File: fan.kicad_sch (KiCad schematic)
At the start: 20 parts, among them J5 Conn_01x04, J6 Conn_01x04, U15 TMP1075, U16 TMP1075, U17 EMC2302, U18 EMC2101

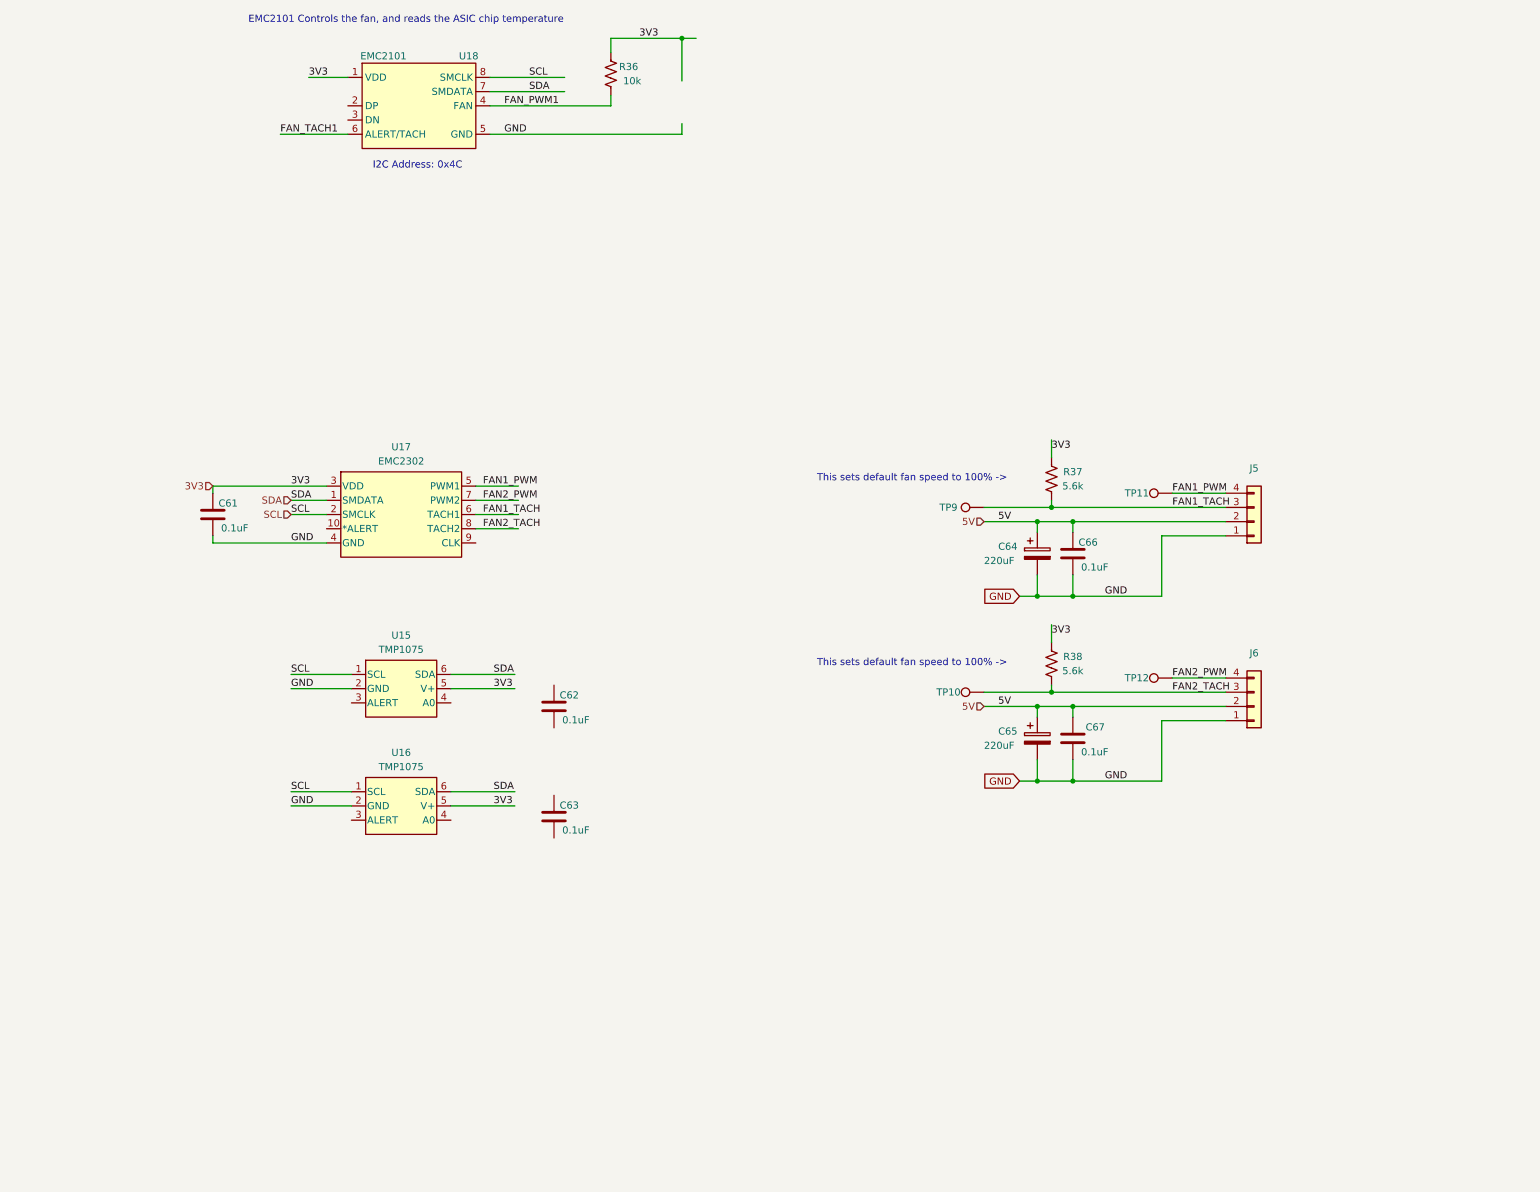
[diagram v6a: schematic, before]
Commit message: add level translator circuits to ASIC communications
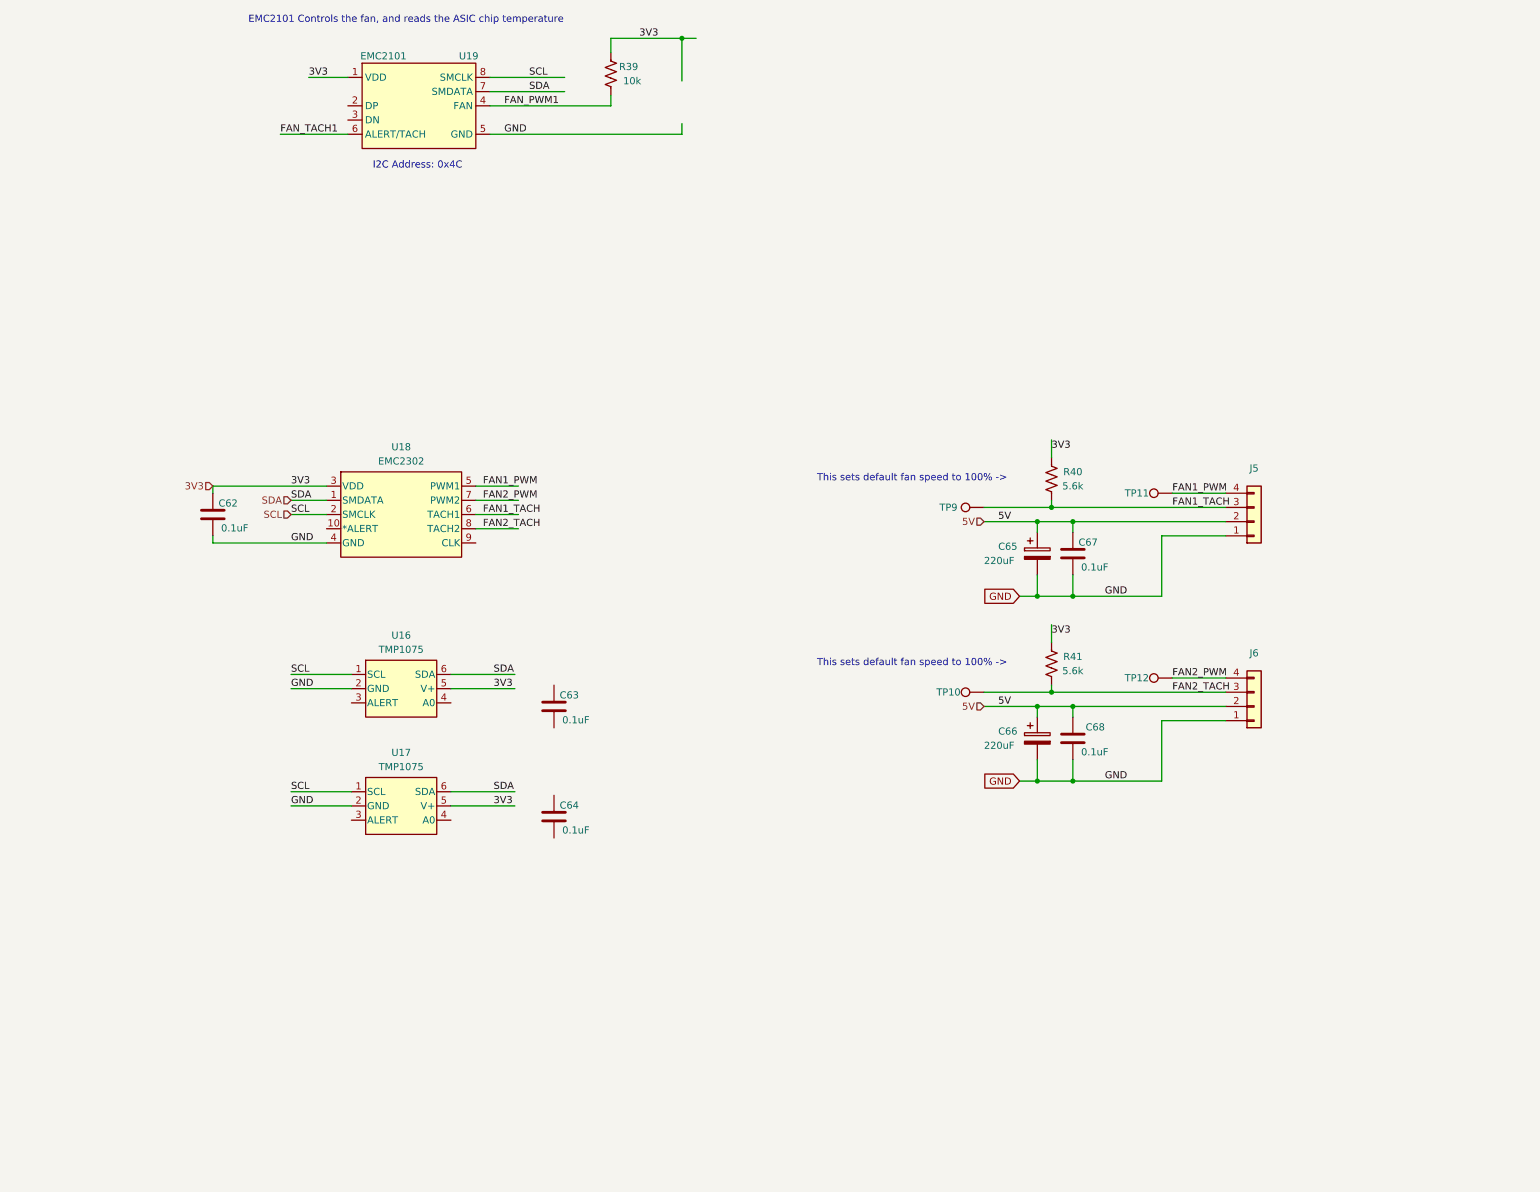
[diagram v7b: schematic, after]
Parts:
- renumbered C61 to C62, C62 to C63, C63 to C64, C64 to C65, C65 to C66, C66 to C67, C67 to C68, R36 to R39, R37 to R40, R38 to R41, U15 to U16, U16 to U17, U17 to U18, U18 to U19
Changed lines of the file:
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@@
   (symbol (lib_id "bitaxe:EMC2302-2-AIZL-TR") (at 89.535 52.07 0) (unit 1)
     (in_bom yes) (on_board yes) (dnp no) (fields_autoplaced)
-    (property "Reference" "U17" (at 91.44 40.005 0)
+    (property "Reference" "U18" (at 91.44 40.005 0)
       (effects (font (size 1.27 1.27)))
     )
@@
       (project "bitaxeUltraHex"
         (path "/e63e39d7-6ac0-4ffd-8aa3-1841a4541b55/8e8832ea-6bf1-49d2-b3a5-32a207f555d2"
-          (reference "U17") (unit 1)
+          (reference "U18") (unit 1)
         )
       )
@@
   (symbol (lib_id "Device:C_Polarized") (at 205.105 92.075 0) (unit 1)
     (in_bom yes) (on_board yes) (dnp no)
-    (property "Reference" "C65" (at 198.12 90.805 0)
+    (property "Reference" "C66" (at 198.12 90.805 0)
       (effects (font (size 1.27 1.27)) (justify left))
     )
@@
       (project "bitaxeUltraHex"
         (path "/e63e39d7-6ac0-4ffd-8aa3-1841a4541b55/8e8832ea-6bf1-49d2-b3a5-32a207f555d2"
-          (reference "C65") (unit 1)
+          (reference "C66") (unit 1)
         )
       )
@@
   (symbol (lib_id "Device:R_US") (at 207.645 45.72 180) (unit 1)
     (in_bom yes) (on_board yes) (dnp no)
-    (property "Reference" "R37" (at 211.455 44.45 0)
+    (property "Reference" "R40" (at 211.455 44.45 0)
       (effects (font (size 1.27 1.27)))
     )
@@
       (project "bitaxeUltraHex"
         (path "/e63e39d7-6ac0-4ffd-8aa3-1841a4541b55/8e8832ea-6bf1-49d2-b3a5-32a207f555d2"
-          (reference "R37") (unit 1)
+          (reference "R40") (unit 1)
         )
       )
@@
   (symbol (lib_id "Device:C") (at 118.745 86.36 0) (mirror y) (unit 1)
     (in_bom yes) (on_board yes) (dnp no)
-    (property "Reference" "C62" (at 123.19 85.09 0)
+    (property "Reference" "C63" (at 123.19 85.09 0)
       (effects (font (size 1.27 1.27)) (justify left bottom))
     )
@@
       (project "bitaxeUltraHex"
         (path "/e63e39d7-6ac0-4ffd-8aa3-1841a4541b55/8e8832ea-6bf1-49d2-b3a5-32a207f555d2"
-          (reference "C62") (unit 1)
+          (reference "C63") (unit 1)
         )
       )
@@
   (symbol (lib_id "Device:C") (at 57.785 52.07 0) (mirror y) (unit 1)
     (in_bom yes) (on_board yes) (dnp no)
-    (property "Reference" "C61" (at 62.23 50.8 0)
+    (property "Reference" "C62" (at 62.23 50.8 0)
       (effects (font (size 1.27 1.27)) (justify left bottom))
     )
@@
       (project "bitaxeUltraHex"
         (path "/e63e39d7-6ac0-4ffd-8aa3-1841a4541b55/8e8832ea-6bf1-49d2-b3a5-32a207f555d2"
-          (reference "C61") (unit 1)
+          (reference "C62") (unit 1)
         )
       )
@@
   (symbol (lib_id "Device:C") (at 211.455 59.055 0) (mirror y) (unit 1)
     (in_bom yes) (on_board yes) (dnp no)
-    (property "Reference" "C66" (at 215.9 57.785 0)
+    (property "Reference" "C67" (at 215.9 57.785 0)
       (effects (font (size 1.27 1.27)) (justify left bottom))
     )
@@
       (project "bitaxeUltraHex"
         (path "/e63e39d7-6ac0-4ffd-8aa3-1841a4541b55/8e8832ea-6bf1-49d2-b3a5-32a207f555d2"
-          (reference "C66") (unit 1)
+          (reference "C67") (unit 1)
         )
       )
@@
   (symbol (lib_id "Device:C") (at 211.455 92.075 0) (mirror y) (unit 1)
     (in_bom yes) (on_board yes) (dnp no)
-    (property "Reference" "C67" (at 217.17 90.805 0)
+    (property "Reference" "C68" (at 217.17 90.805 0)
       (effects (font (size 1.27 1.27)) (justify left bottom))
     )
@@
       (project "bitaxeUltraHex"
         (path "/e63e39d7-6ac0-4ffd-8aa3-1841a4541b55/8e8832ea-6bf1-49d2-b3a5-32a207f555d2"
-          (reference "C67") (unit 1)
+          (reference "C68") (unit 1)
         )
       )
@@
   (symbol (lib_id "Device:R_US") (at 207.645 78.74 180) (unit 1)
     (in_bom yes) (on_board yes) (dnp no)
-    (property "Reference" "R38" (at 211.455 77.47 0)
+    (property "Reference" "R41" (at 211.455 77.47 0)
       (effects (font (size 1.27 1.27)))
     )
@@
       (project "bitaxeUltraHex"
         (path "/e63e39d7-6ac0-4ffd-8aa3-1841a4541b55/8e8832ea-6bf1-49d2-b3a5-32a207f555d2"
-          (reference "R38") (unit 1)
+          (reference "R41") (unit 1)
         )
       )
@@
   (symbol (lib_id "bitaxe:TMP1075NDRLR") (at 71.12 104.14 0) (unit 1)
     (in_bom yes) (on_board yes) (dnp no) (fields_autoplaced)
-    (property "Reference" "U16" (at 91.44 94.615 0)
+    (property "Reference" "U17" (at 91.44 94.615 0)
       (effects (font (size 1.27 1.27)))
     )
@@
       (project "bitaxeUltraHex"
         (path "/e63e39d7-6ac0-4ffd-8aa3-1841a4541b55/8e8832ea-6bf1-49d2-b3a5-32a207f555d2"
-          (reference "U16") (unit 1)
+          (reference "U17") (unit 1)
         )
       )
@@
   (symbol (lib_id "Device:C") (at 118.745 106.045 0) (mirror y) (unit 1)
     (in_bom yes) (on_board yes) (dnp no)
-    (property "Reference" "C63" (at 123.19 104.775 0)
+    (property "Reference" "C64" (at 123.19 104.775 0)
       (effects (font (size 1.27 1.27)) (justify left bottom))
     )
@@
       (project "bitaxeUltraHex"
         (path "/e63e39d7-6ac0-4ffd-8aa3-1841a4541b55/8e8832ea-6bf1-49d2-b3a5-32a207f555d2"
-          (reference "C63") (unit 1)
+          (reference "C64") (unit 1)
         )
       )
@@
   (symbol (lib_name "TMP1075NDRLR_1") (lib_id "bitaxe:TMP1075NDRLR") (at 71.12 83.185 0) (unit 1)
     (in_bom yes) (on_board yes) (dnp no) (fields_autoplaced)
-    (property "Reference" "U15" (at 91.44 73.66 0)
+    (property "Reference" "U16" (at 91.44 73.66 0)
       (effects (font (size 1.27 1.27)))
     )
@@
       (project "bitaxeUltraHex"
         (path "/e63e39d7-6ac0-4ffd-8aa3-1841a4541b55/8e8832ea-6bf1-49d2-b3a5-32a207f555d2"
-          (reference "U15") (unit 1)
+          (reference "U16") (unit 1)
         )
       )
@@
   (symbol (lib_id "Device:C_Polarized") (at 205.105 59.055 0) (unit 1)
     (in_bom yes) (on_board yes) (dnp no)
-    (property "Reference" "C64" (at 198.12 57.785 0)
+    (property "Reference" "C65" (at 198.12 57.785 0)
       (effects (font (size 1.27 1.27)) (justify left))
     )
@@
       (project "bitaxeUltraHex"
         (path "/e63e39d7-6ac0-4ffd-8aa3-1841a4541b55/8e8832ea-6bf1-49d2-b3a5-32a207f555d2"
-          (reference "C64") (unit 1)
+          (reference "C65") (unit 1)
         )
       )
@@
   (symbol (lib_id "Device:R_US") (at 128.905 -26.67 180) (unit 1)
     (in_bom yes) (on_board yes) (dnp no)
-    (property "Reference" "R36" (at 132.08 -27.94 0)
+    (property "Reference" "R39" (at 132.08 -27.94 0)
       (effects (font (size 1.27 1.27)))
     )
@@
       (project "bitaxeUltraHex"
         (path "/e63e39d7-6ac0-4ffd-8aa3-1841a4541b55/8e8832ea-6bf1-49d2-b3a5-32a207f555d2"
-          (reference "R36") (unit 1)
+          (reference "R39") (unit 1)
         )
       )
@@
   (symbol (lib_id "dayminer:EMC2101") (at 94.615 -20.955 0) (unit 1)
     (in_bom yes) (on_board yes) (dnp no)
-    (property "Reference" "U18" (at 103.505 -29.845 0)
+    (property "Reference" "U19" (at 103.505 -29.845 0)
       (effects (font (size 1.27 1.27)))
     )
@@
       (project "bitaxeUltraHex"
         (path "/e63e39d7-6ac0-4ffd-8aa3-1841a4541b55/8e8832ea-6bf1-49d2-b3a5-32a207f555d2"
-          (reference "U18") (unit 1)
-        )
-      )
+          (reference "U19") (unit 1)
+        )
+      )

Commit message: Update temperature sensors, start deep review
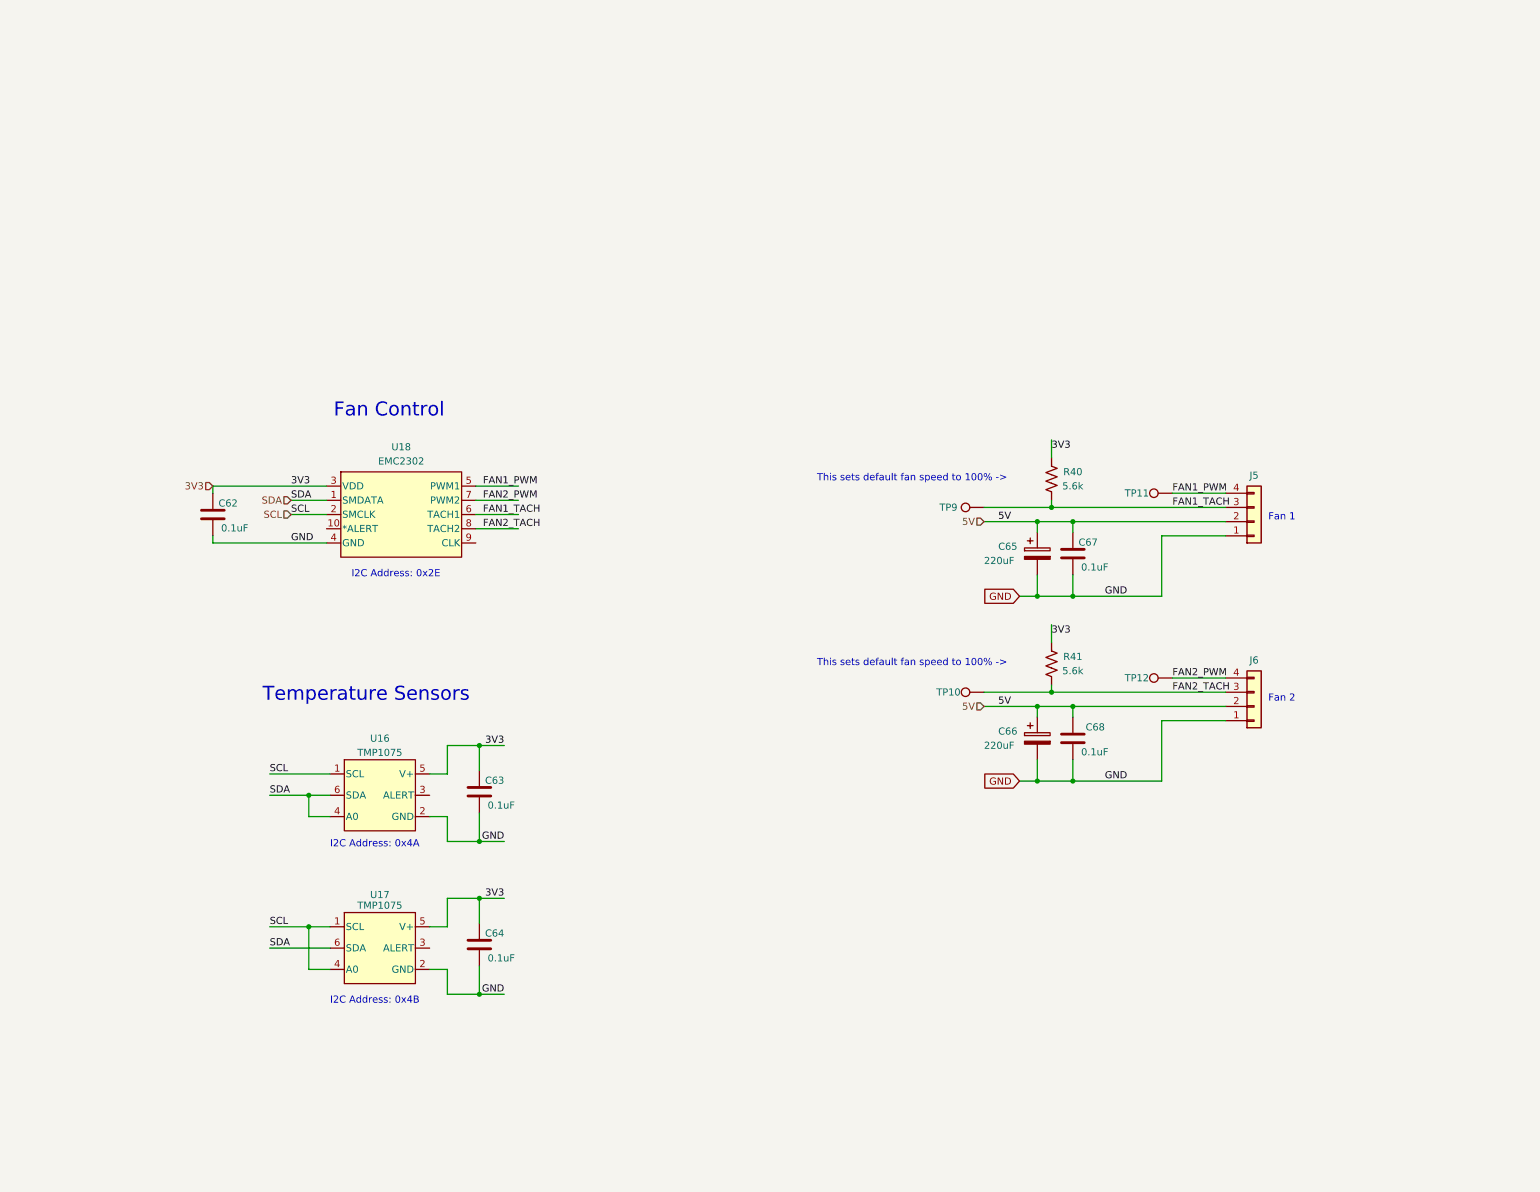
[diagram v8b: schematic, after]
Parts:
- removed R39: 10k, Resistor_SMD:R_0402_1005Metric, symbol Device:R_US
- removed U19: EMC2101, Package_SO:TSSOP-8_3x3mm_P0.65mm, symbol dayminer:EMC2101
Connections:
- net 3V3: now also C63.1, C64.1
- net GND: now also C63.2, C64.2
- net SCL: now also U17.4 (A0)
- net SDA: now also U16.4 (A0)
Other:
- note added: "Fan 1"
- note added: "Fan 2"
- note added: "Fan Control"
- note added: "I2C Address: 0x2E"
- note added: "I2C Address: 0x4A"
- note added: "I2C Address: 0x4B"
- note added: "Temperature Sensors"
- note removed: "EMC2101 Controls the fan, and reads the ASIC chip temperature"
- note removed: "I2C Address: 0x4C"
- moved on the sheet: C63, C64, U16, U17
